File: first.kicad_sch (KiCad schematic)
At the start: 46 parts, among them J1 Conn_01x02_Socket, J10 Conn_01x03_Socket, J11 Conn_01x02_Socket, J2 USB_C_Receptacle_USB2.0_16P, J3 Conn_01x03_Socket, J4 Conn_01x03_Socket, J5 Conn_01x03_Socket, J6 Conn_01x03_Socket, J7 Conn_01x03_Socket, J8 Conn_01x03_Socket, J9 Conn_01x03_Socket, SW1 SW_Push, SW2 SW_DIP_x01, U1 STM32F446RETx, U2 BD33FC0FP, U3 CH340E, U4 MCP2561-E-SN, U5 BD50FC0FP

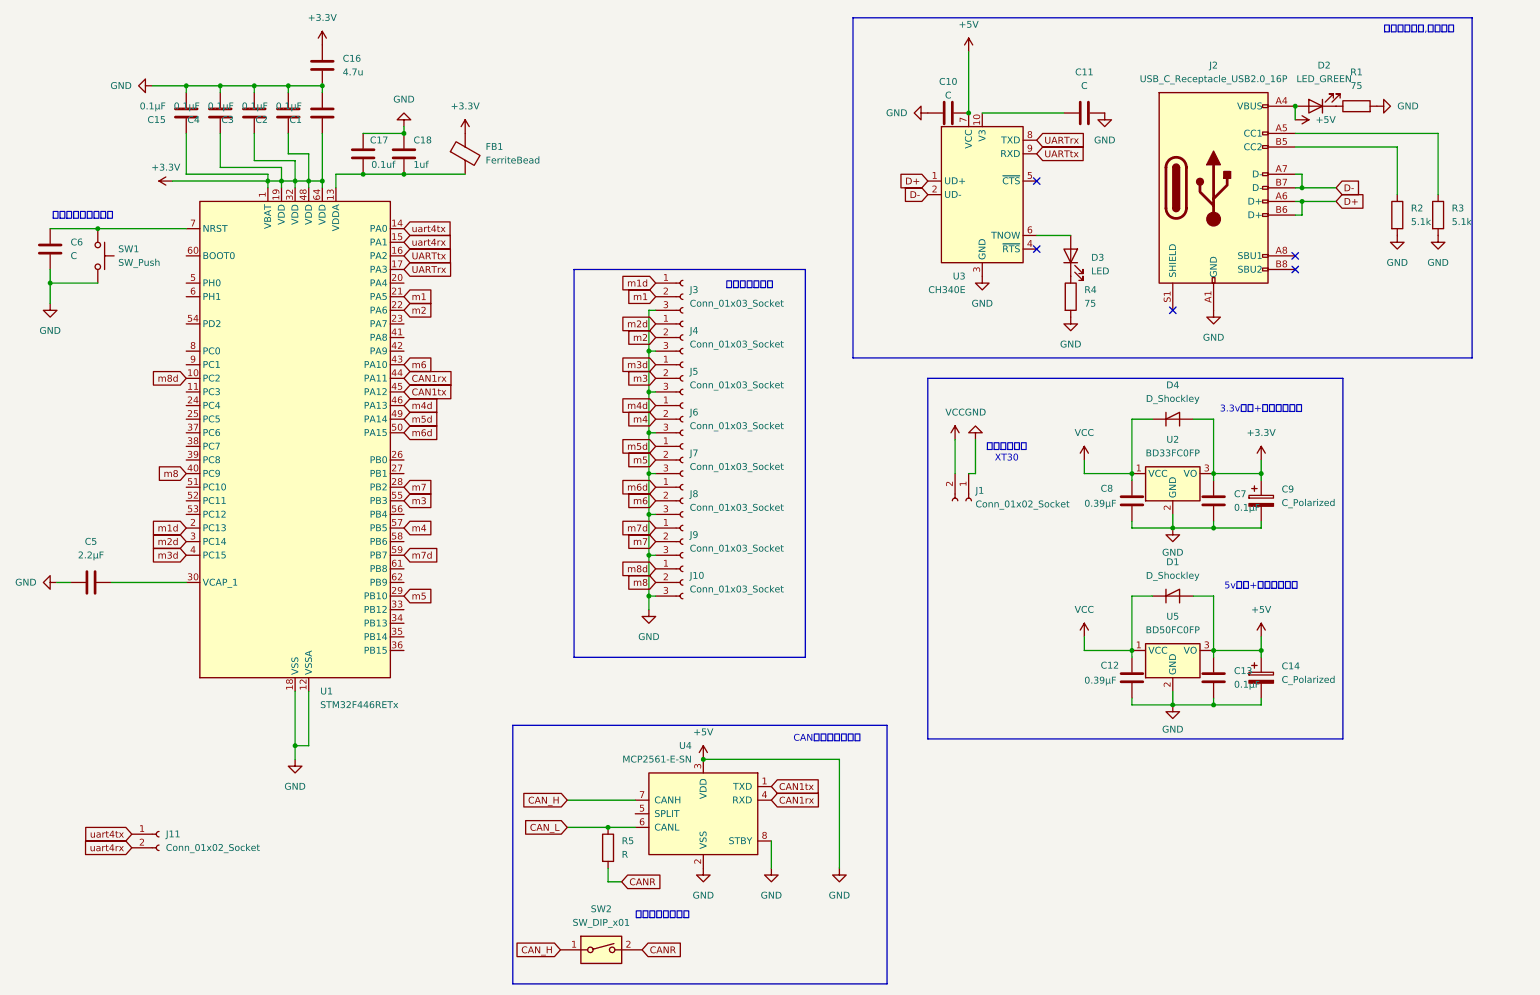
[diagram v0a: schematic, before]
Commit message: フットプリントの割り当てと一部コンデンサの容量の変更 電コンとショッキーダイオードの選定が終わっていない
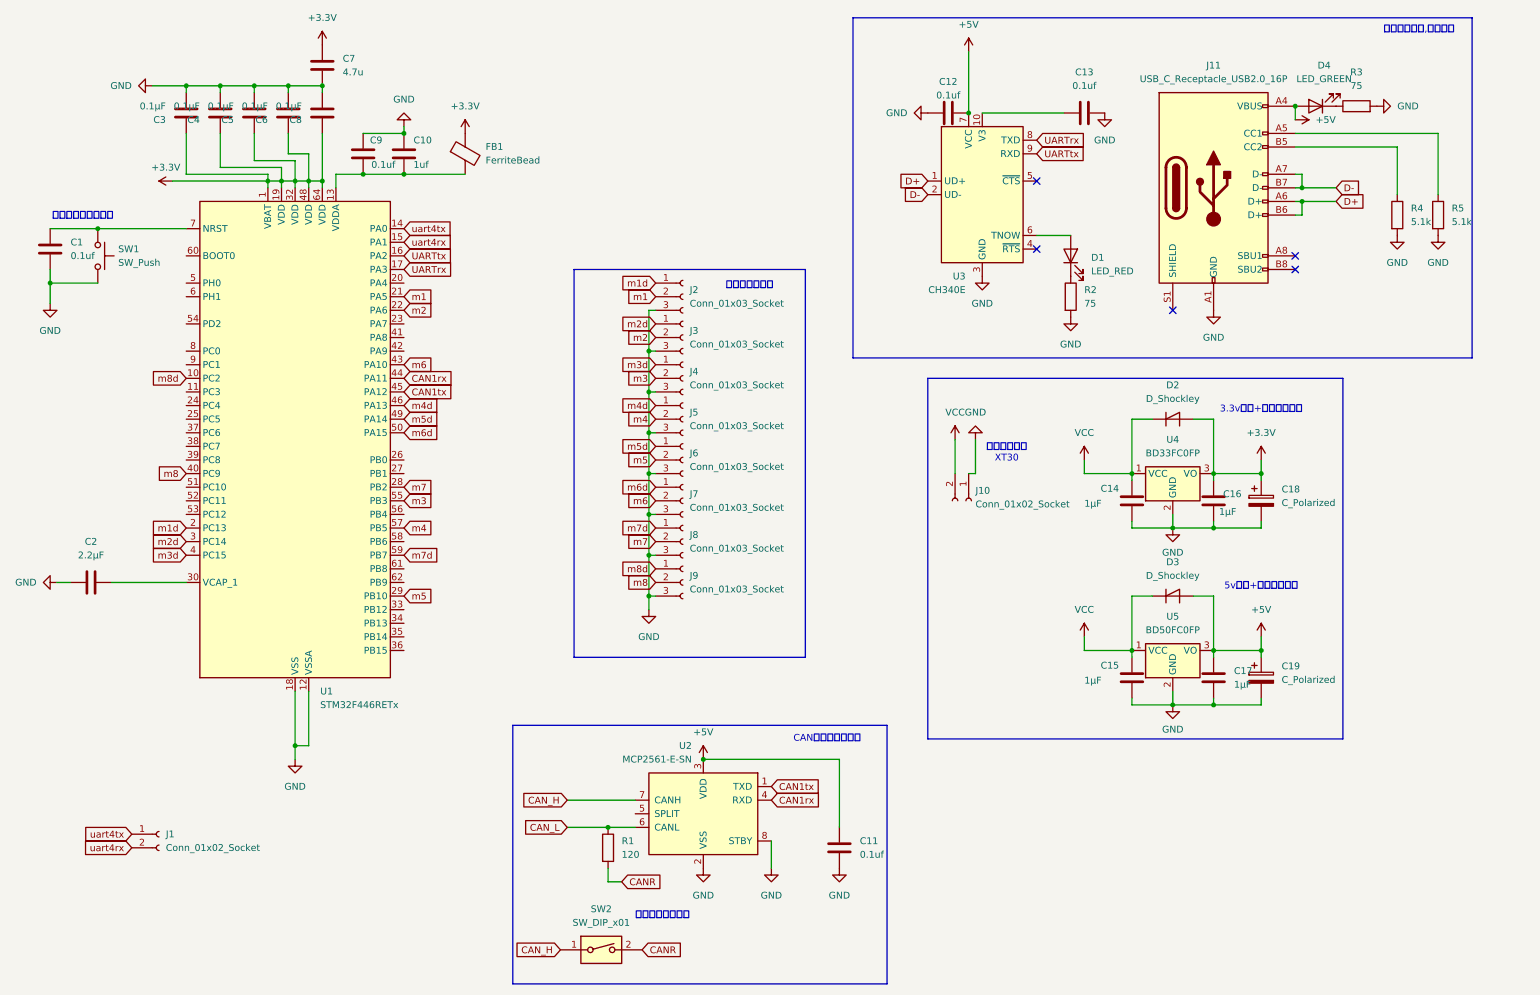
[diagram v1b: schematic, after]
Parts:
- added C11: 0.1uf, Capacitor_SMD:C_0603_1608Metric, symbol Device:C
- C1: renamed from C6; value C -> 0.1uf; footprint (none) -> Capacitor_SMD:C_0603_1608Metric
- C10: renamed from C18; footprint (none) -> Capacitor_SMD:C_0603_1608Metric
- C12: renamed from C10; value C -> 0.1uf; footprint (none) -> Capacitor_SMD:C_0603_1608Metric
- C13: renamed from C11; value C -> 0.1uf; footprint (none) -> Capacitor_SMD:C_0603_1608Metric
- C14: renamed from C8; value 0.39μF -> 1μF; footprint (none) -> Capacitor_SMD:C_0603_1608Metric
- C15: renamed from C12; value 0.39μF -> 1μF; footprint (none) -> Capacitor_SMD:C_0603_1608Metric
- C16: renamed from C7; value 0.1μF -> 1μF; footprint (none) -> Capacitor_SMD:C_0603_1608Metric
- C17: renamed from C13; value 0.1μF -> 1μF; footprint (none) -> Capacitor_SMD:C_0603_1608Metric
- C2: renamed from C5; footprint (none) -> Capacitor_SMD:C_0603_1608Metric
- C3: renamed from C15; footprint (none) -> Capacitor_SMD:C_0603_1608Metric
- C4: footprint (none) -> Capacitor_SMD:C_0603_1608Metric
- C5: renamed from C3; footprint (none) -> Capacitor_SMD:C_0603_1608Metric
- C6: renamed from C2; footprint (none) -> Capacitor_SMD:C_0603_1608Metric
- C7: renamed from C16; footprint (none) -> Capacitor_SMD:C_0805_2012Metric
- C8: renamed from C1; footprint (none) -> Capacitor_SMD:C_0603_1608Metric
- C9: renamed from C17; footprint (none) -> Capacitor_SMD:C_0603_1608Metric
- D1: renamed from D3; value LED -> LED_RED; footprint (none) -> Diode_SMD:D_0603_1608Metric
- D4: renamed from D2; footprint (none) -> Diode_SMD:D_0603_1608Metric
- FB1: footprint (none) -> Inductor_SMD:L_0603_1608Metric
- R1: renamed from R5; value R -> 120; footprint (none) -> Resistor_SMD:R_0805_2012Metric
- R2: renamed from R4; footprint (none) -> Resistor_SMD:R_0603_1608Metric
- R3: renamed from R1; footprint (none) -> Resistor_SMD:R_0603_1608Metric
- R4: renamed from R2; footprint (none) -> Resistor_SMD:R_1206_3216Metric
- R5: renamed from R3; footprint (none) -> Resistor_SMD:R_1206_3216Metric
- renumbered C9 to C18, C14 to C19, D4 to D2, D1 to D3, J11 to J1, J1 to J10, J2 to J11, J3 to J2, J4 to J3, J5 to J4, J6 to J5, J7 to J6, J8 to J7, J9 to J8, J10 to J9, U4 to U2, U2 to U4
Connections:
- net +5V: now also C11.1; no longer C1.2, C10.1, C12.1, C13.2, C14.2, C15.2, C16.2, C17.2, C18.2, C19.2, C2.1, C3.2, C4.2, C5.2, C6.2, C7.2, C8.2, C9.1, J10.1 (Pin_1), J11.A1 (GND), J11.A12 (GND), J11.B1 (GND), J11.B12 (GND), J2.3 (Pin_3), J3.3 (Pin_3), J4.3 (Pin_3), J5.3 (Pin_3), J6.3 (Pin_3), J7.3 (Pin_3), J8.3 (Pin_3), J9.3 (Pin_3), R2.2, R3.2, R4.2, R5.2, SW1.2, U1.12 (VSSA), U1.18 (VSS), U1.31 (VSS), U1.47 (VSS), U1.63 (VSS), U2.2 (VSS), U2.8 (STBY), U3.3 (GND), U4.2 (GND), U5.2 (GND)
- new net GND: C1.2, C10.1, C11.2, C12.1, C13.2, C14.2, C15.2, C16.2, C17.2, C18.2, C19.2, C2.1, C3.2, C4.2, C5.2, C6.2, C7.2, C8.2, C9.1, J10.1 (Pin_1), J11.A1 (GND), J11.A12 (GND), J11.B1 (GND), J11.B12 (GND), J2.3 (Pin_3), J3.3 (Pin_3), J4.3 (Pin_3), J5.3 (Pin_3), J6.3 (Pin_3), J7.3 (Pin_3), J8.3 (Pin_3), J9.3 (Pin_3), R2.2, R3.2, R4.2, R5.2, SW1.2, U1.12 (VSSA), U1.18 (VSS), U1.31 (VSS), U1.47 (VSS), U1.63 (VSS), U2.2 (VSS), U2.8 (STBY), U3.3 (GND), U4.2 (GND), U5.2 (GND)

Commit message: 回路図を描き終えた
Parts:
- removed SW2: SW_DIP_x01, symbol Switch:SW_DIP_x01
- added SW3: SW_Wuerth_450301014042, Button_Switch_THT:SW_Slide-03_Wuerth-WS-SLTV_10x2.5x6.4_P2.54mm, symbol Switch:SW_Wuerth_450301014042
- C1, C10, C11, C12, C13, C2, C3, C4, C5, C6, C8, C9: footprint Capacitor_SMD:C_0603_1608Metric -> Capacitor_SMD:C_0603_1608Metric_Pad1.08x0.95mm_HandSolder
- C14, C15, C16, C17: value 1μF -> 4.7μF; footprint Capacitor_SMD:C_0603_1608Metric -> Capacitor_SMD:C_0805_2012Metric_Pad1.18x1.45mm_HandSolder
- C18, C19: footprint (none) -> Capacitor_SMD:C_Elec_6.3x7.7
- C7: value 4.7u -> 4.7uf; footprint Capacitor_SMD:C_0805_2012Metric -> Capacitor_SMD:C_0603_1608Metric_Pad1.08x0.95mm_HandSolder
- D1, D4: footprint Diode_SMD:D_0603_1608Metric -> Diode_SMD:D_0603_1608Metric_Pad1.05x0.95mm_HandSolder
- D2, D3: footprint (none) -> Diode_SMD:D_SOD-882
- FB1: footprint Inductor_SMD:L_0603_1608Metric -> Inductor_SMD:L_0603_1608Metric_Pad1.05x0.95mm_HandSolder
- R1: footprint Resistor_SMD:R_0805_2012Metric -> Resistor_SMD:R_0805_2012Metric_Pad1.20x1.40mm_HandSolder
- R2, R3: footprint Resistor_SMD:R_0603_1608Metric -> Resistor_SMD:R_0603_1608Metric_Pad0.98x0.95mm_HandSolder
- R4, R5: footprint Resistor_SMD:R_1206_3216Metric -> Resistor_SMD:R_1206_3216Metric_Pad1.30x1.75mm_HandSolder
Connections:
- net CANR: now also SW3.3 (A)
- net CAN_H: now also SW3.1 (B)
- net m7: now also U1.27 (PB1); no longer U1.28 (PB2)
- net m8: now also U1.26 (PB0); no longer U1.40 (PC9)
- no-connect marks 5 -> 6

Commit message: pcbの配置のみを行った 配線は地獄
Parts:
- added H1, H2, H3, H4: MountingHole, MountingHole:MountingHole_3.2mm_M3, symbol Mechanical:MountingHole
- added J12: Conn_01x03_Socket, Connector_JST:JST_XH_S3B-XH-A-1_1x03_P2.50mm_Horizontal, symbol Connector:Conn_01x03_Socket
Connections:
- net CAN_H: now also J12.3 (Pin_3)
- net CAN_L: now also J12.1 (Pin_1)
- net GND: now also J12.2 (Pin_2)

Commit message: 次のコミット時に記入
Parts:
- C18: value C_Polarized -> 22uf
- C2: value 2.2μF -> 4.7μF
- D1: value LED_RED -> LED_GREEN
- D4: value LED_GREEN -> LED_RED
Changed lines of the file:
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@@
 	(text "終端抵抗オンオフ"
 		(exclude_from_sim no)
-		(at 141.224 183.896 0)
+		(at 127.762 179.07 0)
 		(effects
 			(font
@@
 			)
 		)
-		(property "Value" "C_Polarized"
+		(property "Value" "22uf"
 			(at 247.65 104.5209 0)
 			(effects
@@
 			)
 		)
-		(property "Value" "LED_GREEN"
+		(property "Value" "LED_RED"
 			(at 255.5875 25.4 0)
 			(effects
@@
 			)
 		)
-		(property "Value" "LED_RED"
+		(property "Value" "LED_GREEN"
 			(at 212.09 61.2774 90)
 			(effects
@@
 			)
 		)
-		(property "Value" "2.2μF"
+		(property "Value" "4.7μF"
 			(at 25.4 114.3 90)
 			(effects

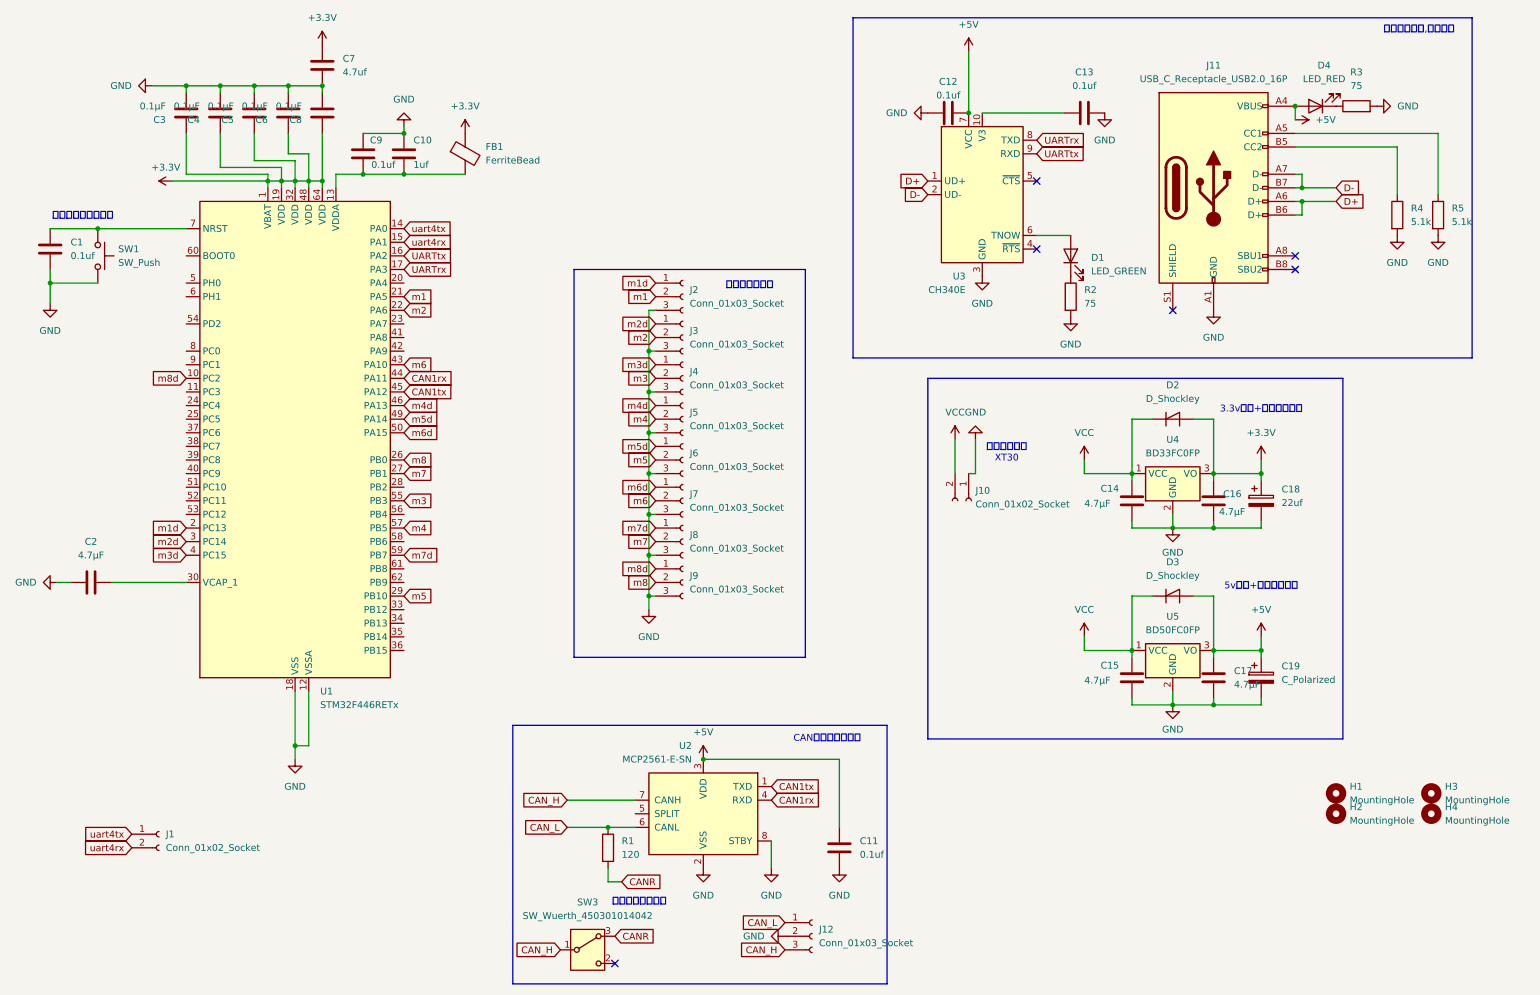
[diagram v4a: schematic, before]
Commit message: 回路図の一部素子の変更、削除。pcbの電源回りの配線
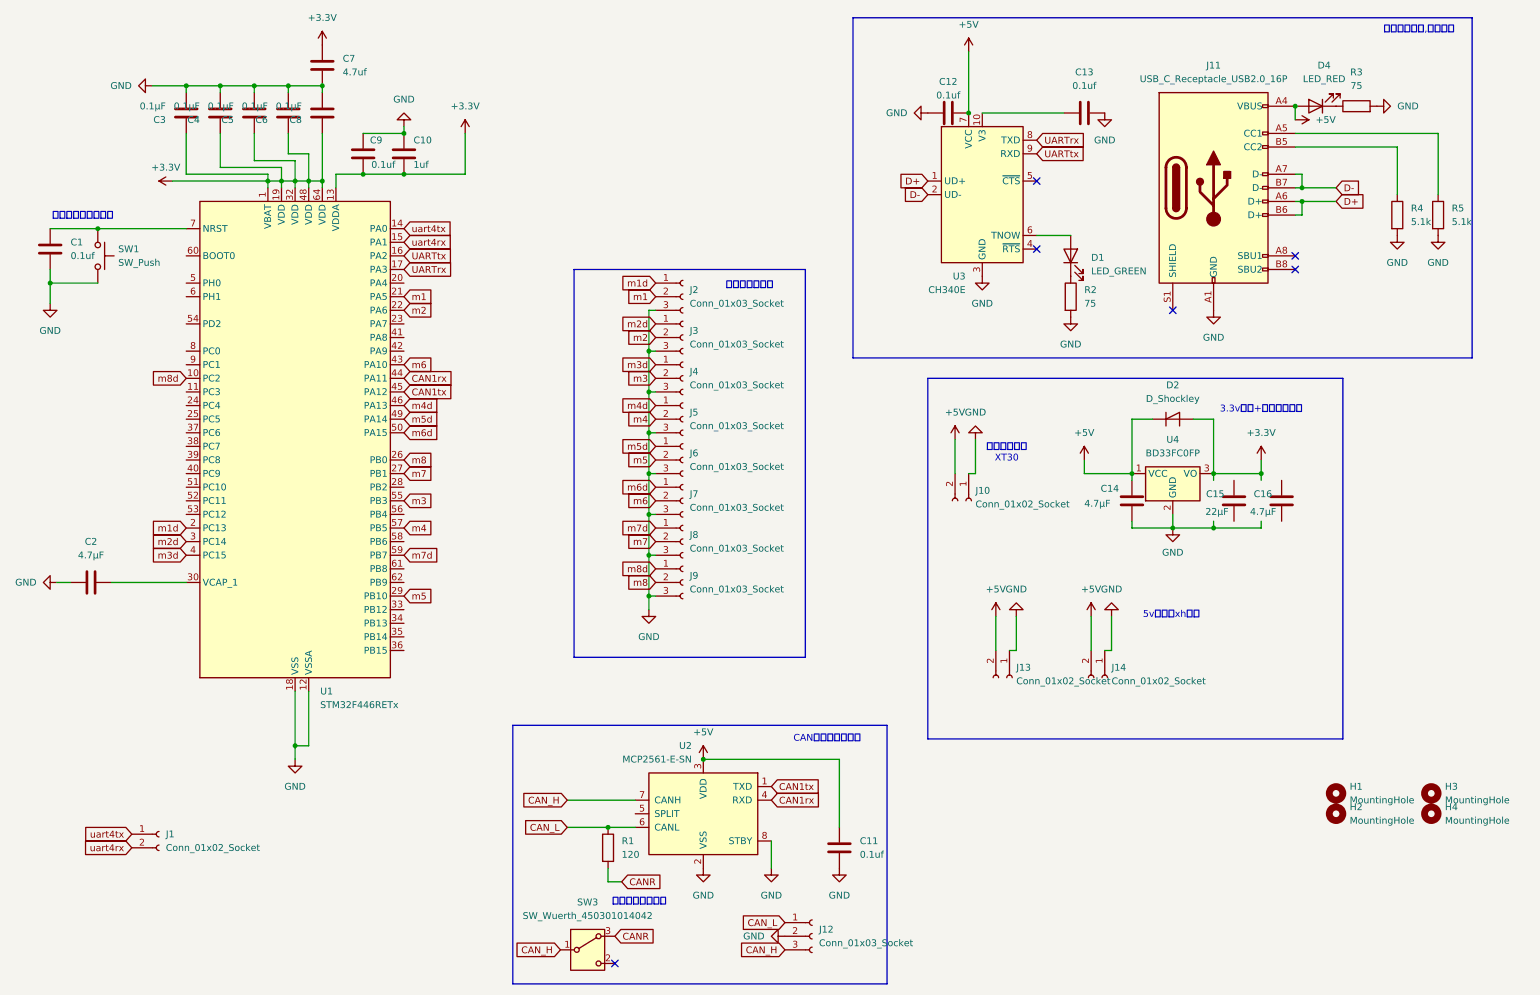
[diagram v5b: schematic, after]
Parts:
- removed C17: 4.7μF, Capacitor_SMD:C_0805_2012Metric_Pad1.18x1.45mm_HandSolder, symbol Device:C
- removed C18: 22uf, Capacitor_SMD:C_Elec_6.3x7.7, symbol Device:C_Polarized
- removed C19: C_Polarized, Capacitor_SMD:C_Elec_6.3x7.7, symbol Device:C_Polarized
- removed D3: D_Shockley, Diode_SMD:D_SOD-882, symbol Device:D_Shockley
- removed FB1: FerriteBead, Inductor_SMD:L_0603_1608Metric_Pad1.05x0.95mm_HandSolder, symbol Device:FerriteBead
- removed U5: BD50FC0FP, Package_TO_SOT_SMD:TO-252-2, symbol Regulator_Linear:BD50FC0FP
- added J13, J14: Conn_01x02_Socket, Connector_JST:JST_XH_S2B-XH-A-1_1x02_P2.50mm_Horizontal, symbol Connector:Conn_01x02_Socket
- C15: value 4.7μF -> 22μF
- C3, C4, C5, C6, C8, C9: footprint Capacitor_SMD:C_0603_1608Metric_Pad1.08x0.95mm_HandSolder -> Capacitor_SMD:C_0201_0603Metric_Pad0.64x0.40mm_HandSolder
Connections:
- net +3.3V: now also C10.2, C9.2, U1.13 (VDDA); no longer C16.1
- net +5V: now also C14.1, D2.1 (K), J10.2 (Pin_2), U4.1 (VCC), J13.2 (Pin_2), J14.2 (Pin_2)
- net GND: now also J13.1 (Pin_1), J14.1 (Pin_1); no longer C15.2, C16.2
- removed net VCC: C14.1, C15.1, D2.1 (K), J10.2 (Pin_2), U4.1 (VCC)
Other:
- note added: "5v供給用xh端子"
- note removed: "5v変圧+逆流防止回路"
- moved on the sheet: C16
